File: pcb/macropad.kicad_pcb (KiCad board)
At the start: 2 copper layers, 40.5 x 69.1 mm, 7 parts, among them SW1 SW_Push, SW2 SW_Push, SW3 SW_Push, SW4 SW_Push, U1 XIAO-RP2040-DIP

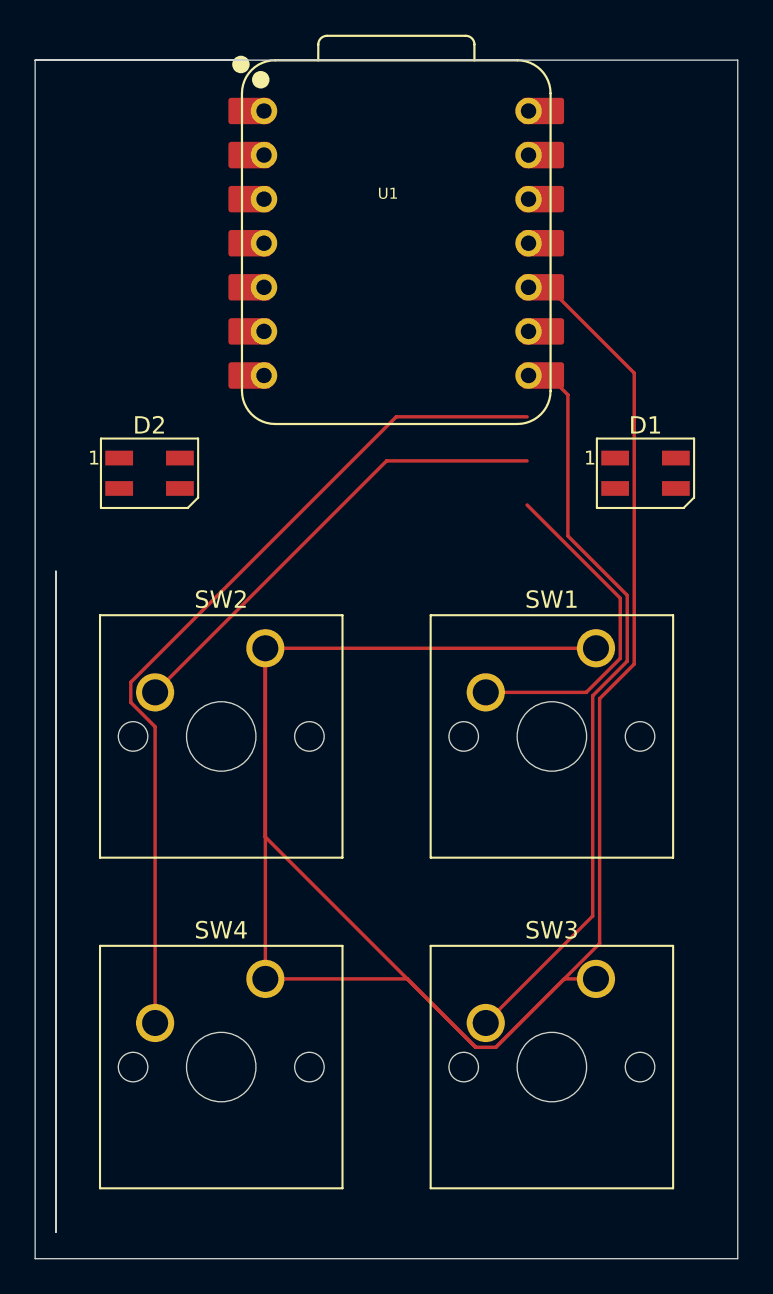
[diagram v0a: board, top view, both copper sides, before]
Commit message: Finalised PCB
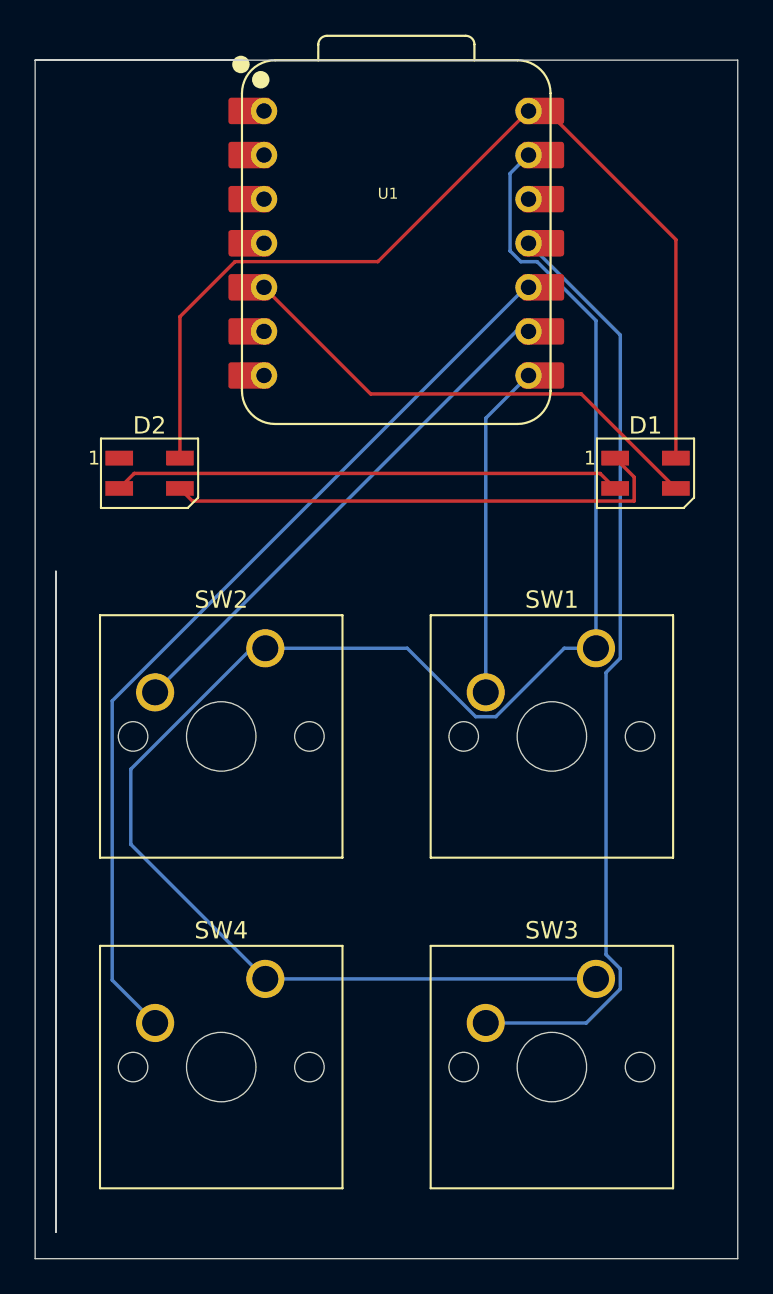
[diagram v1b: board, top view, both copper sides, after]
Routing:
- net +5V: track 0.00 -> 57.3 mm
- net GND: track 138.9 -> 98.8 mm
- net Net-(D1-DOUT): track 0.00 -> 29.4 mm
- net Net-(D1-VSS): track 0.00 -> 29.3 mm
- net Net-(D1-DIN): track 0.00 -> 28.5 mm
- net Net-(U1-GPIO3/MOSI): track 43.9 -> 54.4 mm
- net Net-(U1-GPIO4/MISO): track 49.4 -> 54.5 mm
- net Net-(U1-GPIO2/SCK): track 27.0 -> 30.1 mm
- net Net-(U1-GPIO1/RX): track 20.6 -> 21.4 mm
